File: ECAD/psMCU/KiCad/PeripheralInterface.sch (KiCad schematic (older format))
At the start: 24 parts, among them J6 PERIPH_INTERFACE, U26 SN74HC245PW, U27 SN74HC245PW, U28 SN74LVC1G86DCK, U29 SN74HC245PW, U30 SN74LVC1G04DCK, U349 SN74LVC1G08DCK, U350 SN74LVC1G08DCK, U351 SN74LVC1G08DCK

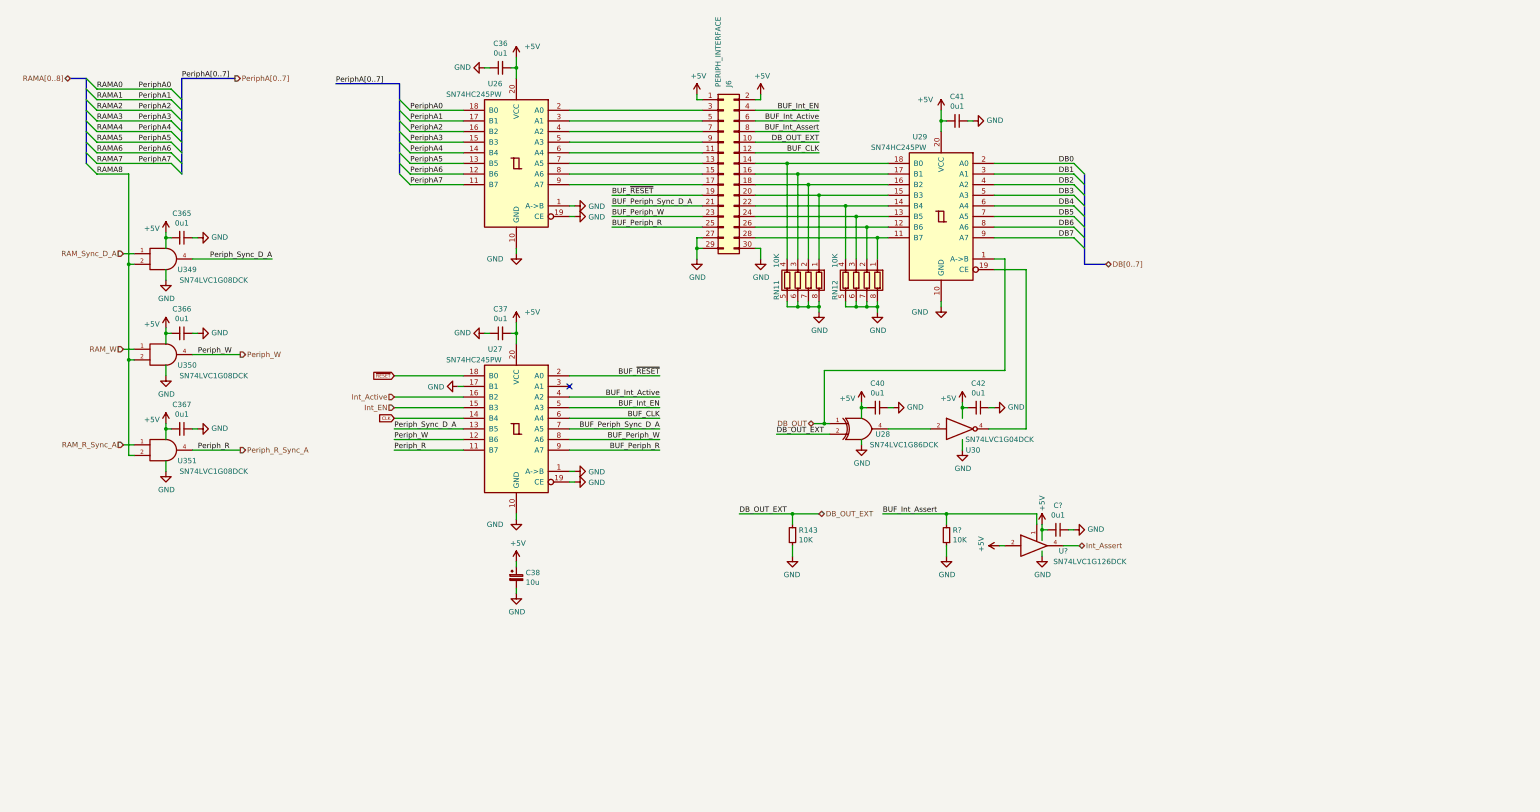
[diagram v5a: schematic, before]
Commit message: Sch: Modified instruction set to add fast memory access functions.
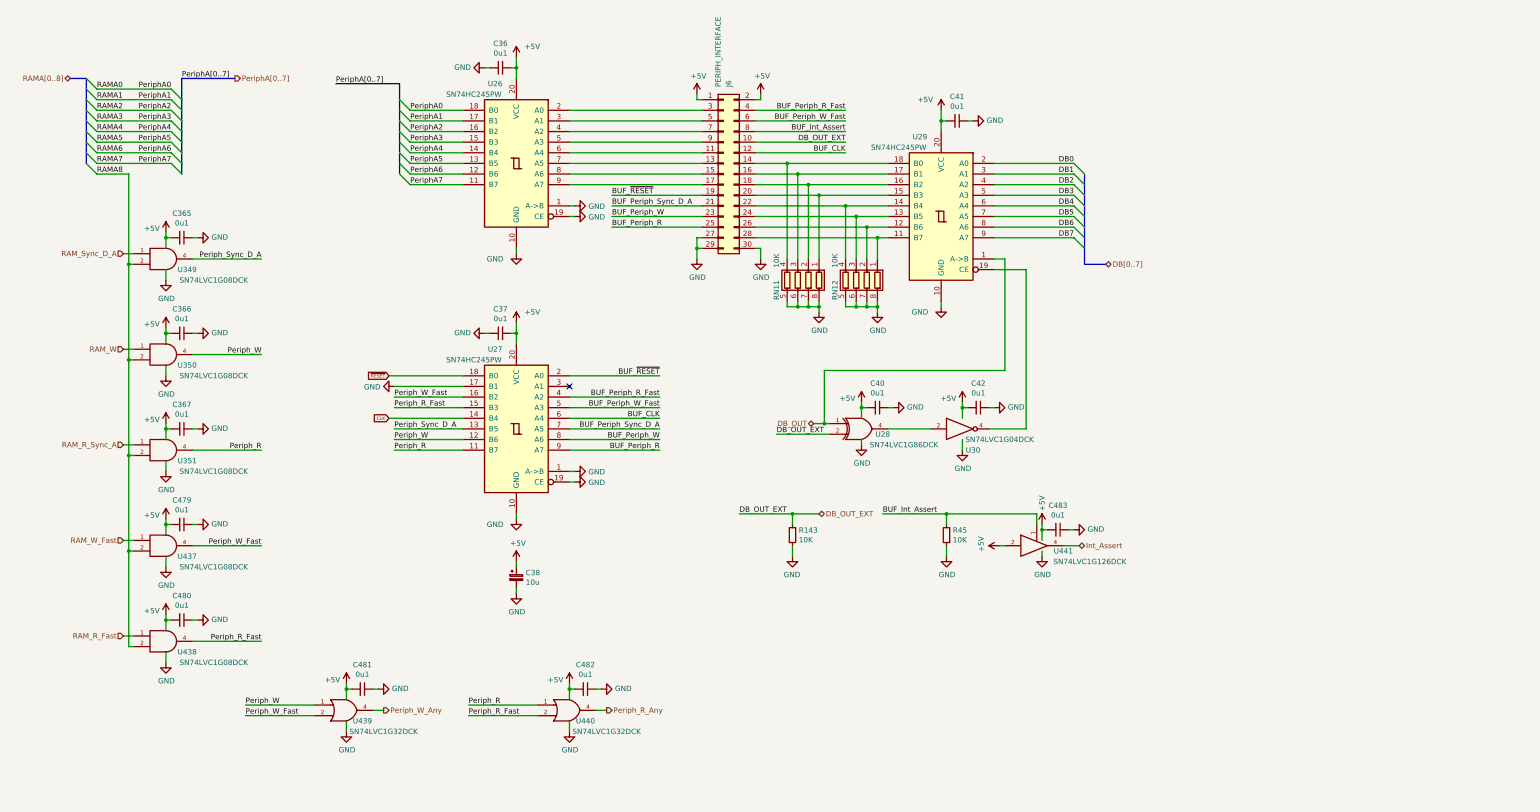
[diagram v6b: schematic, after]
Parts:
- added C479, C480, C481, C482: 0u1, NoRef_Footprints:C_0603_1608Metric_NoRef, symbol Device:C_Small
- added U437, U438: SN74LVC1G08DCK, Package_TO_SOT_SMD:SOT-353_SC-70-5, symbol 74xGxx:74LVC1G08
- added U439, U440: SN74LVC1G32DCK, Package_TO_SOT_SMD:SOT-353_SC-70-5, symbol 74xGxx:74LVC1G32
- gave numbers to parts that had none: 3
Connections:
- net +5V: now also C479.2, C480.2, C481.2, C482.2, U437.5 (VCC), U438.5 (VCC), U439.5 (VCC), U440.5 (VCC)
- net GND: now also C479.1, C480.1, C481.1, C482.1, U437.3 (GND), U438.3 (GND), U439.3 (GND), U440.3 (GND)
- net Periph_W: now also U439.1
- net RAMA8: now also U437.2, U438.2
- net BUF_Int_Active renamed BUF_Periph_R_Fast
- net BUF_Periph_R_Fast: now also J6.4 (Pin_4); no longer J6.6 (Pin_6)
- net BUF_Int_EN renamed BUF_Periph_W_Fast
- net BUF_Periph_W_Fast: now also J6.6 (Pin_6); no longer J6.4 (Pin_4)
- net Int_Active renamed Periph_W_Fast
- net Periph_W_Fast: now also U437.4, U439.2
- net Int_EN renamed Periph_R_Fast
- net Periph_R_Fast: now also U438.4, U440.2
- net Periph_R_Sync_A renamed Periph_R
- net Periph_R: now also U440.1
- new net Periph_R_Any: U440.4
- new net Periph_W_Any: U439.4
- new net RAM_R_Fast: U438.1
- new net RAM_W_Fast: U437.1

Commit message: Sch: Cleanup + Small fixes
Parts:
- added C502: 0u1, NoRef_Footprints:C_0603_1608Metric_NoRef, symbol Device:C_Small
- added U458: SN74LVC1G126DCK, Package_TO_SOT_SMD:SOT-353_SC-70-5, symbol 74xGxx:74LVC1G126
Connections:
- net +5V: now also C502.2, U458.1, U458.5 (VCC)
- net DB_OUT_EXT: now also U458.2, U458.4
- net GND: now also C502.1, U458.3 (GND)
- net BUF_Int_Assert renamed Int_Assert_EXT
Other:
- note added: "Address Buffer"
- note added: "All Periphs. fall into the address space 0x100 - 0x1ff.\nBy disabeling the read/write and related control signals when\nthe address is outside of this range, peripherals only have to\ncheck the first 8 bits of the currently selected address."
- note added: "All internal peripherals (SYS1-3, TEMP1-2) support both fast and slow access.\nThe fast and slow control lines are combined here for all of these registers, \nto avoid duplicate circuitry."
- note added: "Bidirectional, changes direction \nbased on which DB_OUT signal \n(Internal or external) is active."
- note added: "Control Line Buffer"
- note added: "Databus Buffer"
- note added: "Internal Peripheral Control Signals"
- note added: "Peripheral Connector"
- note added: "Peripheral Control Gating"
- moved on the sheet: C36, C365, C366, C367, C37, C38, C40, C41, C42, C479, C480, C481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
